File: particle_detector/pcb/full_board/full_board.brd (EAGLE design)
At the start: 64 x 32 mm, 43 parts, among them IC1 LT1807R, IC2 TLV3501, IC3 LT3461, IC4 TEENSY 3.2, IC5 SENSL-SIPM

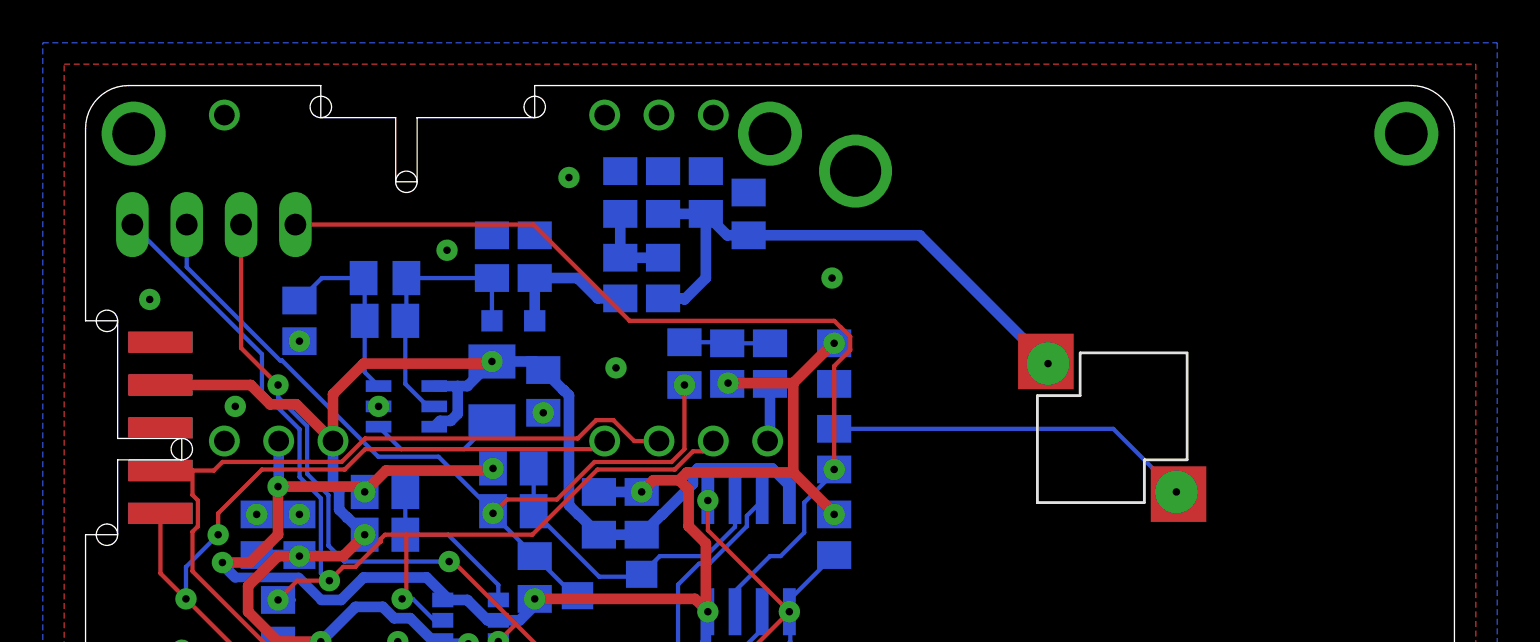
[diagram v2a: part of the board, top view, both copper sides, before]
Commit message: remove empty xbus header, add TX/RX pins to teensy
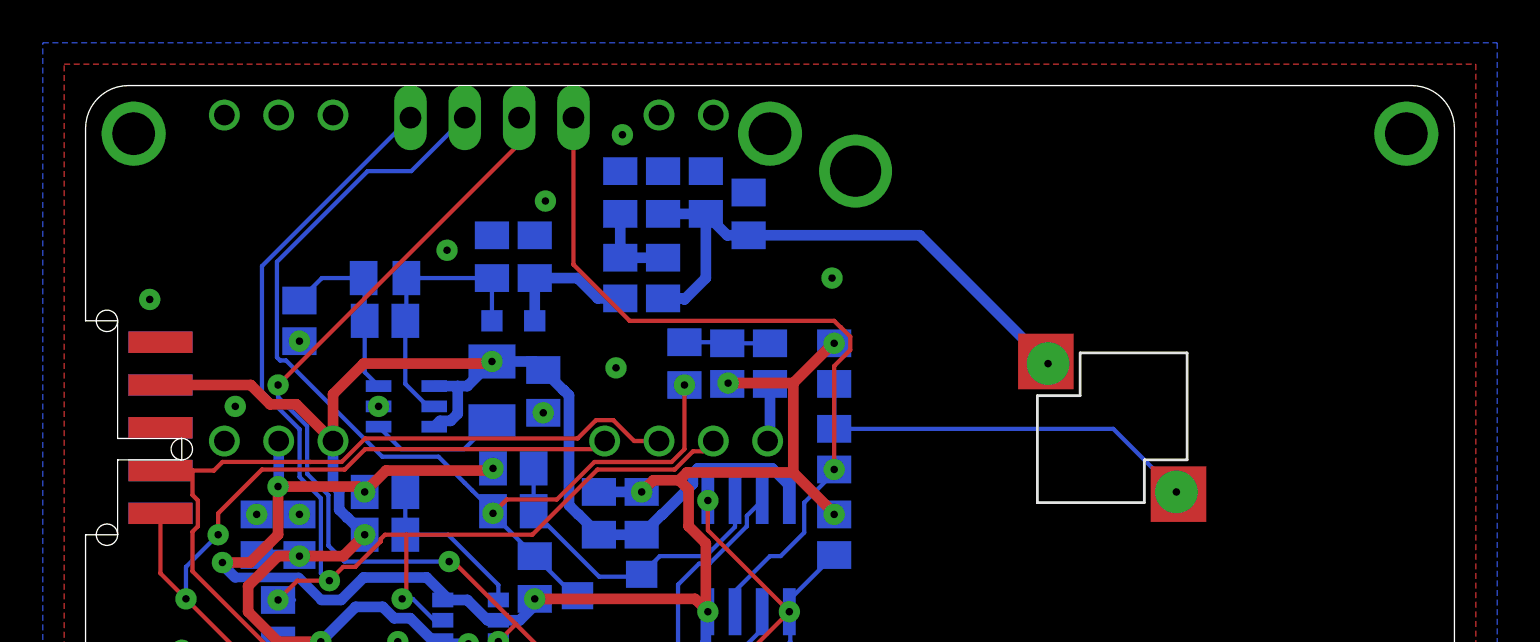
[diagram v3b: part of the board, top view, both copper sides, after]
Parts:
- moved TOUCH 13.9 mm to (19.0, 30.5)
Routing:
- net SIG_AMP: track 59.5 -> 68.4 mm
- net SIG_PEAK: track 40.0 -> 48.0 mm
- net SIG_RAW: track 43.5 -> 36.6 mm
- net SIG_INT: track 50.8 -> 56.1 mm
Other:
- outline, holes or cut-outs redrawn
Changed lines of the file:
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@@
 <wire x1="0" y1="21" x2="0" y2="30" width="0" layer="20"/>
 <wire x1="0" y1="30" x2="2" y2="32" width="0" layer="20" curve="-90"/>
-<wire x1="2" y1="32" x2="11" y2="32" width="0" layer="20"/>
 <wire x1="21" y1="0" x2="62" y2="0" width="0" layer="20"/>
 <wire x1="62" y1="0" x2="64" y2="2" width="0" layer="20" curve="90"/>
 <wire x1="64" y1="2" x2="64" y2="30" width="0" layer="20"/>
 <wire x1="64" y1="30" x2="62" y2="32" width="0" layer="20" curve="90"/>
-<wire x1="62" y1="32" x2="21" y2="32" width="0" layer="20"/>
+<wire x1="62" y1="32" x2="2" y2="32" width="0" layer="20"/>
 <wire x1="0" y1="11" x2="0" y2="2" width="0" layer="20"/>
 <wire x1="0" y1="2" x2="2" y2="0" width="0" layer="20" curve="90"/>
 <wire x1="2" y1="0" x2="11" y2="0" width="0" layer="20"/>
-<text x="9.5" y="27.2" size="0.6" layer="26" ratio="14" rot="MR90">RAW</text>
-<text x="7" y="27.3" size="0.6" layer="26" ratio="14" rot="MR90">AMP</text>
-<text x="4.5" y="27.3" size="0.6" layer="26" ratio="14" rot="MR90">PEAK</text>
+<text x="22.6" y="26.8" size="0.6" layer="26" ratio="14" rot="MR90">RAW</text>
+<text x="20" y="27" size="0.6" layer="26" ratio="14" rot="MR90">AMP</text>
+<text x="17.6" y="26.5" size="0.6" layer="26" ratio="14" rot="MR90">PEAK</text>
 <hole x="1" y="11" drill="1"/>
 <hole x="1" y="21" drill="1"/>
@@
 <dimension x1="64" y1="-7" x2="0" y2="-7" x3="32" y3="-7" textsize="1" layer="47" visible="yes"/>
 <dimension x1="-8" y1="0" x2="-8" y2="32" x3="-8" y3="16" textsize="1" layer="47" visible="yes"/>
-<text x="0.6" y="26.8" size="0.6" layer="26" ratio="14" rot="MR90">INT</text>
-<rectangle x1="36" y1="4" x2="60" y2="28" layer="29" rot="R180"/>
-<hole x="11" y="31" drill="1"/>
-<hole x="21" y="31" drill="1"/>
-<wire x1="11" y1="32" x2="11" y2="30.5" width="0" layer="20"/>
-<wire x1="11" y1="30.5" x2="14.5" y2="30.5" width="0" layer="20"/>
-<wire x1="15.5" y1="30.5" x2="21" y2="30.5" width="0" layer="20"/>
-<wire x1="21" y1="30.5" x2="21" y2="32" width="0" layer="20"/>
-<hole x="15" y="27.5" drill="1"/>
-<wire x1="14.5" y1="30.5" x2="14.5" y2="27.5" width="0" layer="20"/>
-<wire x1="14.5" y1="27.5" x2="15.5" y2="27.5" width="0" layer="20"/>
-<wire x1="15.5" y1="27.5" x2="15.5" y2="30.5" width="0" layer="20"/>
+<text x="14.9" y="27.3" size="0.6" layer="26" ratio="14" rot="MR90">INT</text>
 <hole x="11" y="1" drill="1"/>
 <hole x="21" y="1" drill="1"/>
@@
 <wire x1="14.5" y1="4.5" x2="15.5" y2="4.5" width="0" layer="20"/>
 <wire x1="15.5" y1="4.5" x2="15.5" y2="1.5" width="0" layer="20"/>
-<rectangle x1="11" y1="27" x2="21" y2="32" layer="42" rot="R180"/>
-<rectangle x1="11" y1="27" x2="21" y2="32" layer="41" rot="R180"/>
+<rectangle x1="36" y1="4" x2="43" y2="28" layer="29"/>
+<rectangle x1="53" y1="4" x2="60" y2="28" layer="29"/>
+<rectangle x1="43" y1="21" x2="53" y2="28" layer="29"/>
+<rectangle x1="43" y1="4" x2="53" y2="11" layer="29"/>
 </plain>
 <attributes>
@@
 <attribute name="VALUE" x="11.571" y="15.095" size="0.6" layer="28" rot="MR90"/>
 </element>
-<element name="IC4" library="personal" package="TEENSY_3.2_THINSAT" value="TEENSY 3.2" x="23" y="23" smashed="yes" rot="MR270">
-<attribute name="NAME" x="9.03" y="26.81" size="0.6" layer="26" font="vector" rot="MR270"/>
-</element>
-<element name="TOUCH" library="pinhead" library_urn="urn:adsk.eagle:library:325" package="1X04" package3d_urn="urn:adsk.eagle:package:22407/2" value="" x="6" y="25.5" smashed="yes" rot="MR0">
-<attribute name="VALUE" x="11.08" y="22.325" size="1.27" layer="28" rot="MR0"/>
+<element name="IC4" library="personal" package="TEENSY_3.2_THINSAT" value="TEENSY 3.2" x="23" y="23" smashed="yes" rot="MR270"/>
+<element name="TOUCH" library="pinhead" library_urn="urn:adsk.eagle:library:325" package="1X04" package3d_urn="urn:adsk.eagle:package:22407/2" value="" x="19" y="30.5" smashed="yes" rot="MR0">
+<attribute name="VALUE" x="24.08" y="27.325" size="1.27" layer="28" rot="MR0"/>
 </element>
 <element name="L2" library="rcl" package="L2012C" value="2.5k" x="20" y="21" smashed="yes" rot="MR0">
@@
 <attribute name="NAME" x="25.875" y="26" size="0.6" layer="26" rot="MR90"/>
 <attribute name="SPICEPREFIX" value="C" x="25" y="27" size="1.778" layer="28" rot="MR90" display="off"/>
-<attribute name="VALUE" x="23.1" y="26" size="0.6" layer="28" rot="MR90"/>
+<attribute name="VALUE" x="23.5" y="25.6" size="0.6" layer="28" rot="MR90"/>
 </element>
 <element name="C13" library="rcl" package="C0805K" value="10uF" x="31" y="26" smashed="yes" rot="MR90">
@@
 <via x="14.6" y="6" extent="1-16" drill="0.35" diameter="1"/>
 <via x="16.9" y="24.3" extent="1-16" drill="0.35" diameter="1"/>
-<via x="22.6" y="27.7" extent="1-16" drill="0.35" diameter="1"/>
+<via x="25.1" y="29.7" extent="1-16" drill="0.35" diameter="1"/>
 <via x="34.9" y="23" extent="1-16" drill="0.35" diameter="1"/>
 <via x="24.8" y="18.8" extent="1-16" drill="0.35" diameter="1"/>
+<via x="21.5" y="26.6" extent="1-16" drill="0.35" diameter="1"/>
 </signal>
 <signal name="HV">
@@
 <wire x1="35" y1="14" x2="35" y2="14.05" width="0.2" layer="1"/>
 <via x="35" y="14.05" extent="1-16" drill="0.35" diameter="1"/>
-<wire x1="20.94074375" y1="25.5" x2="9.81" y2="25.5" width="0.2" layer="1"/>
+<wire x1="22.81" y1="23.63074375" x2="22.81" y2="30.5" width="0.2" layer="1"/>
 <wire x1="35.7524" y1="19.63834375" x2="35.7524" y2="20.26165625" width="0.2" layer="1"/>
 <wire x1="35.7524" y1="20.26165625" x2="35.31165625" y2="20.7024" width="0.2" layer="1"/>
@@
 <wire x1="35" y1="18.88594375" x2="35.7524" y2="19.63834375" width="0.2" layer="1"/>
 <wire x1="35" y1="21" x2="25.44074375" y2="21" width="0.2" layer="1"/>
-<wire x1="25.44074375" y1="21" x2="20.94074375" y2="25.5" width="0.2" layer="1"/>
+<wire x1="25.44074375" y1="21" x2="22.81" y2="23.63074375" width="0.2" layer="1"/>
 </signal>
 <signal name="N$8">
@@
 <via x="19.3" y="6.0026" extent="1-16" drill="0.35" diameter="1"/>
 <wire x1="19.3" y1="6.0026" x2="19.3" y2="6.05" width="0.2" layer="16"/>
-<wire x1="7.27" y1="25.5" x2="7.27" y2="19.73" width="0.2" layer="1"/>
-<wire x1="7.27" y1="19.73" x2="9" y2="18" width="0.2" layer="1"/>
+<wire x1="20.27" y1="30.5" x2="20.27" y2="29.27" width="0.2" layer="1"/>
+<wire x1="9" y1="18" x2="20.27" y2="29.27" width="0.2" layer="1"/>
 <via x="9" y="18" extent="1-16" drill="0.35" diameter="1"/>
 <wire x1="32.905" y1="7.4" x2="29.095" y2="11.21" width="0.2" layer="1"/>
@@
 <via x="19.05" y="12" extent="1-16" drill="0.35" diameter="1"/>
 <wire x1="28" y1="18" x2="28" y2="15" width="0.2" layer="1"/>
-<wire x1="19.05" y1="12.1" x2="16.5024" y2="14.6476" width="0.2" layer="16"/>
-<wire x1="16.5024" y1="14.6476" x2="13.6831" y2="14.6476" width="0.2" layer="16"/>
-<wire x1="9.1831" y1="19.1476" x2="9.09545" y2="19.1476" width="0.2" layer="16"/>
-<wire x1="9.09545" y1="19.1476" x2="4.73" y2="23.51305" width="0.2" layer="16"/>
-<wire x1="13.6831" y1="14.6476" x2="9.1831" y2="19.1476" width="0.2" layer="16"/>
-<wire x1="4.73" y1="23.51305" x2="4.73" y2="25.5" width="0.2" layer="16"/>
+<wire x1="17.73" y1="13.42" x2="18.075" y2="13.075" width="0.2" layer="16"/>
+<wire x1="18.075" y1="13.075" x2="19.05" y2="12.1" width="0.2" layer="16"/>
 <wire x1="22.035975" y1="12.6476" x2="19.6976" y2="12.6476" width="0.2" layer="1"/>
 <wire x1="19.05" y1="12" x2="19.6976" y2="12.6476" width="0.2" layer="1"/>
@@
 <wire x1="27.4" y1="14.4" x2="28" y2="15" width="0.2" layer="1"/>
 <wire x1="23.788375" y1="14.4" x2="27.4" y2="14.4" width="0.2" layer="1"/>
+<wire x1="17.73" y1="30.5" x2="15.23" y2="28" width="0.2" layer="16"/>
+<wire x1="15.23" y1="28" x2="13.188375" y2="28" width="0.2" layer="16"/>
+<wire x1="8.9476" y1="23.759225" x2="13.188375" y2="28" width="0.2" layer="16"/>
+<wire x1="17.73" y1="13.42" x2="16.5024" y2="14.6476" width="0.2" layer="16"/>
+<wire x1="9.09545" y1="19.1476" x2="8.9476" y2="19.29545" width="0.2" layer="16"/>
+<wire x1="9.37045" y1="19.1476" x2="9.09545" y2="19.1476" width="0.2" layer="16"/>
+<wire x1="16.5024" y1="14.6476" x2="13.87045" y2="14.6476" width="0.2" layer="16"/>
+<wire x1="13.87045" y1="14.6476" x2="9.37045" y2="19.1476" width="0.2" layer="16"/>
+<wire x1="8.9476" y1="19.29545" x2="8.9476" y2="23.759225" width="0.2" layer="16"/>
 </signal>
 <signal name="N$9">
@@
 <wire x1="28.398375" y1="14.9" x2="27.545975" y2="14.0476" width="0.2" layer="1"/>
 <wire x1="28.87" y1="14.9" x2="28.398375" y2="14.9" width="0.2" layer="1"/>
-<wire x1="8.2476" y1="19.4424" x2="8.2476" y2="17.68834375" width="0.2" layer="16"/>
+<wire x1="8.2476" y1="23.5576" x2="8.2476" y2="17.68834375" width="0.2" layer="16"/>
 <wire x1="8.2476" y1="17.68834375" x2="10.0063" y2="15.92964375" width="0.2" layer="16"/>
 <wire x1="11.0024" y1="9.1976" x2="11.4" y2="8.8" width="0.2" layer="16"/>
@@
 <wire x1="11.4" y1="8.8" x2="11.4" y2="8.8524" width="0.2" layer="16"/>
 <via x="11.4" y="8.8524" extent="1-16" drill="0.35" diameter="1"/>
-<wire x1="2.19" y1="25.5" x2="8.2476" y2="19.4424" width="0.2" layer="16"/>
+<wire x1="15.19" y1="30.5" x2="8.2476" y2="23.5576" width="0.2" layer="16"/>
 <wire x1="9" y1="7.95" x2="9.9024" y2="8.8524" width="0.2" layer="1"/>
 <wire x1="9.9024" y1="8.8524" x2="11.4" y2="8.8524" width="0.2" layer="1"/>

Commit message: swap teensy for new teensy pinout with TX/RX
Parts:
- turned XBUS1 to 270 degrees
- turned XBUS2 to 180 degrees
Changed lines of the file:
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@@
 <attribute name="VALUE" x="27.46" y="17.73" size="0.6" layer="28" rot="MR90"/>
 </element>
-<element name="XBUS1" library="personal" package="XBUS_2X05_PAD" value="" x="3.5" y="16" smashed="yes" rot="R90">
-<attribute name="VALUE" x="6.675" y="11.92" size="1.27" layer="27" rot="R90"/>
+<element name="XBUS1" library="personal" package="XBUS_2X05_PAD" value="" x="3.5" y="16" smashed="yes" rot="R270">
+<attribute name="VALUE" x="0.325" y="20.08" size="1.27" layer="27" rot="R270"/>
 </element>
 <element name="L1" library="rcl" library_urn="urn:adsk.eagle:library:334" package="L3225M" package3d_urn="urn:adsk.eagle:package:23477/1" value="47uH" x="19" y="17.7" smashed="yes" rot="MR270">
@@
 <attribute name="VALUE" x="37.54" y="20.27" size="0.6" layer="28" rot="MR270"/>
 </element>
-<element name="XBUS2" library="personal" package="XBUS_2X05_PAD" value="" x="16" y="3.4" smashed="yes">
-<attribute name="VALUE" x="11.92" y="0.225" size="1.27" layer="27"/>
+<element name="XBUS2" library="personal" package="XBUS_2X05_PAD" value="" x="16" y="3.4" smashed="yes" rot="R180">
+<attribute name="VALUE" x="20.08" y="6.575" size="1.27" layer="27" rot="R180"/>
 </element>
 </elements>

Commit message: layout TX/RX and change power to 5V; send to PCBWay 2019.05.29
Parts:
- moved IC2 1.10 mm to (18.0, 8.10)
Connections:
- removed net VBAT: XBUS1.5, XBUS2.5
- removed net VCC: IC4.VIN
- new net 5V: IC4.VIN, XBUS1.5, XBUS2.5
- new net RX: IC4.0, XBUS1.8, XBUS2.8
- new net TX: IC4.1, XBUS1.9, XBUS2.9
- net 3.3V: no longer XBUS1.4, XBUS2.4
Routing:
- net TX: track 0.00 -> 50.4 mm, vias 0 -> 3
- net RX: track 0.00 -> 47.7 mm
- net 5V: track 0.00 -> 32.5 mm, vias 0 -> 1
- net 3.3V: track 77.7 -> 63.8 mm, vias 5 -> 4
- net SCL: track 37.8 -> 39.1 mm
- net SDA: track 41.7 -> 42.6 mm
- net N$5: track 8.02 -> 7.16 mm
- net SIG_AMP: track 68.4 -> 67.6 mm
- net AGND: track 78.9 -> 78.4 mm

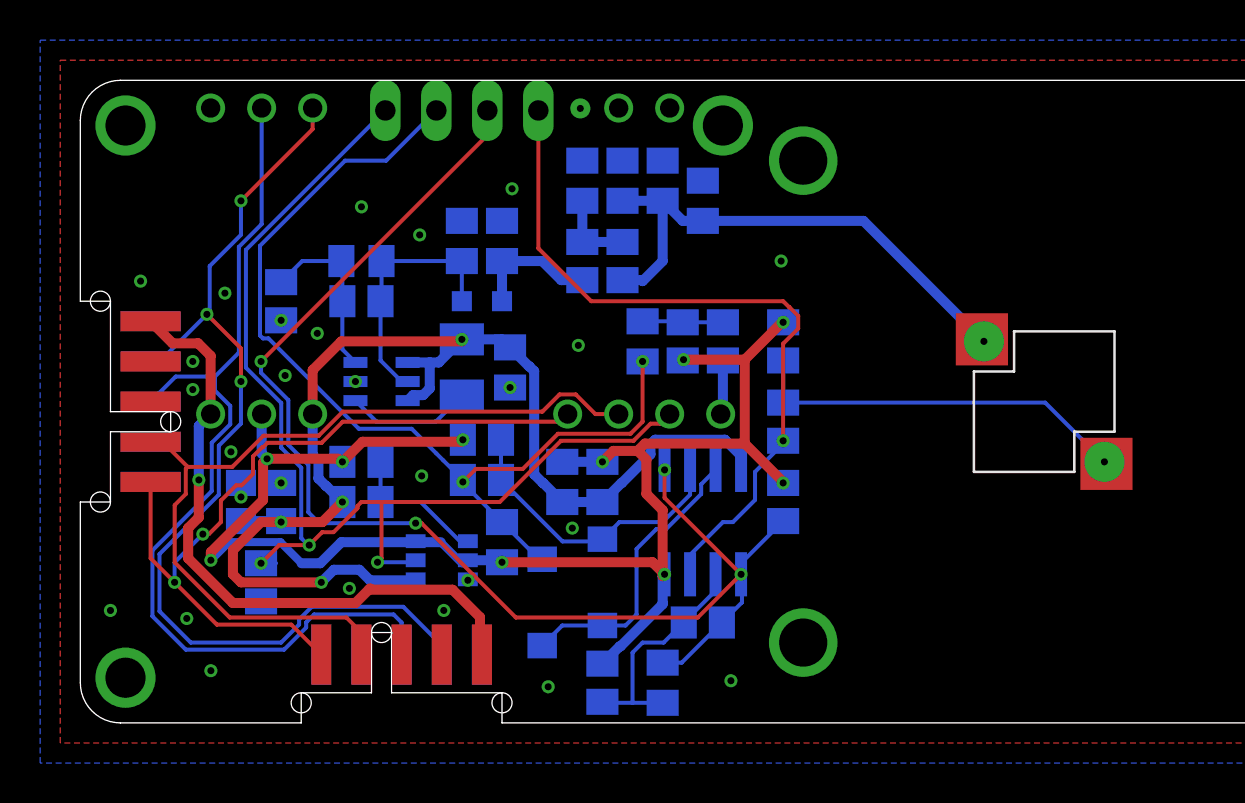
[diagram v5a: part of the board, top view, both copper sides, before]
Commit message: begin conforming to mechanical keepout spec
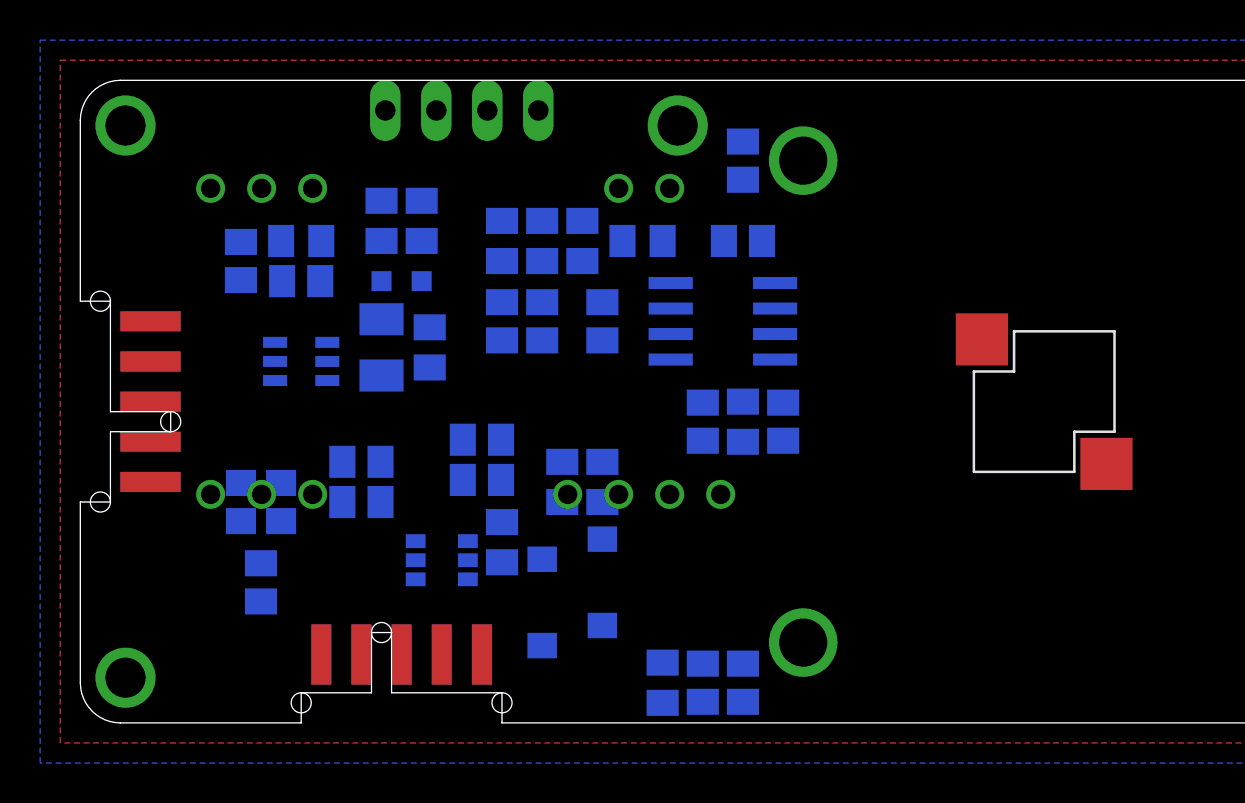
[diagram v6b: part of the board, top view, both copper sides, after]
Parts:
- moved C9 17.0 mm to (29.0, 2.00)
- moved R10 17.0 mm to (33.0, 2.00)
- moved R9 17.0 mm to (31.0, 2.00)
- moved R4 13.9 mm to (31.0, 15.0)
- moved C5 13.6 mm to (33.0, 15.0)
- moved R3 13.2 mm to (33.0, 28.0), turned to 90 degrees
- moved R6 12.7 mm to (26.0, 20.0)
- moved R5 10.8 mm to (35.0, 15.0), turned to 270 degrees
- moved IC1 10.0 mm to (32.0, 20.0), turned to 270 degrees
- moved R16 5.39 mm to (33.0, 24.0), turned to 0 degrees
- moved C12 5.00 mm to (21.0, 24.0)
- moved C14 5.00 mm to (25.0, 24.0)
- moved C15 5.00 mm to (23.0, 24.0)
- moved R14 5.00 mm to (21.0, 20.0)
- moved R15 5.00 mm to (23.0, 20.0), turned to 90 degrees
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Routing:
- net AGND: track 78.4 -> 0.00 mm, vias 10 -> 0
- net SIG_AMP: track 67.6 -> 0.00 mm, vias 5 -> 0
- net 3.3V: track 63.8 -> 0.00 mm, vias 4 -> 0
- net SIG_INT: track 55.8 -> 0.00 mm, vias 3 -> 0
- net TX: track 50.4 -> 0.46 mm, vias 3 -> 0
- net SIG_PEAK: track 48.0 -> 0.00 mm, vias 2 -> 0
- net RX: track 47.7 -> 0.00 mm
- net SDA: track 42.6 -> 0.60 mm
- net SCL: track 39.1 -> 0.00 mm, vias 2 -> 0
- net SIG_RAW: track 36.6 -> 0.00 mm, vias 1 -> 0
- net 5V: track 32.5 -> 0.00 mm, vias 1 -> 0
- net N$6: track 26.5 -> 0.00 mm, vias 1 -> 0
- net SIGNAL: track 20.4 -> 0.00 mm, vias 1 -> 0
- net N$4: track 14.9 -> 0.00 mm
- net N$2: track 14.5 -> 0.00 mm
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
